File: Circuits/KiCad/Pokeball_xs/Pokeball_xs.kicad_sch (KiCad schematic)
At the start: 21 parts

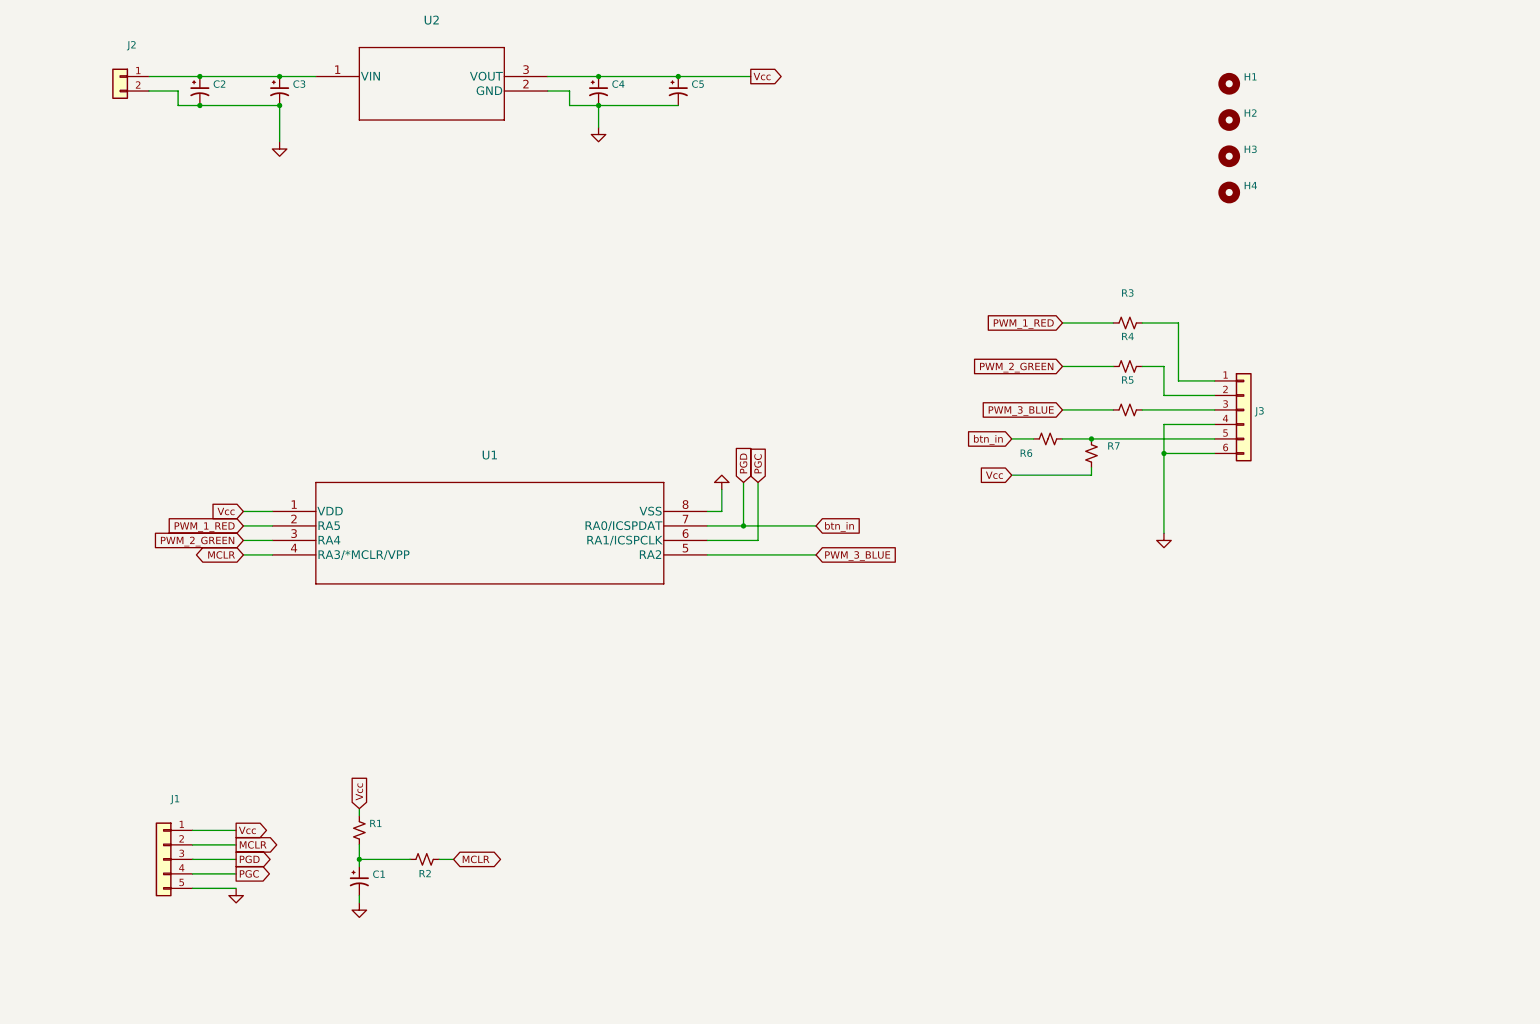
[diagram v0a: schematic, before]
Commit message: v 0.0.0.1 - Include the charging circuit on the PCB
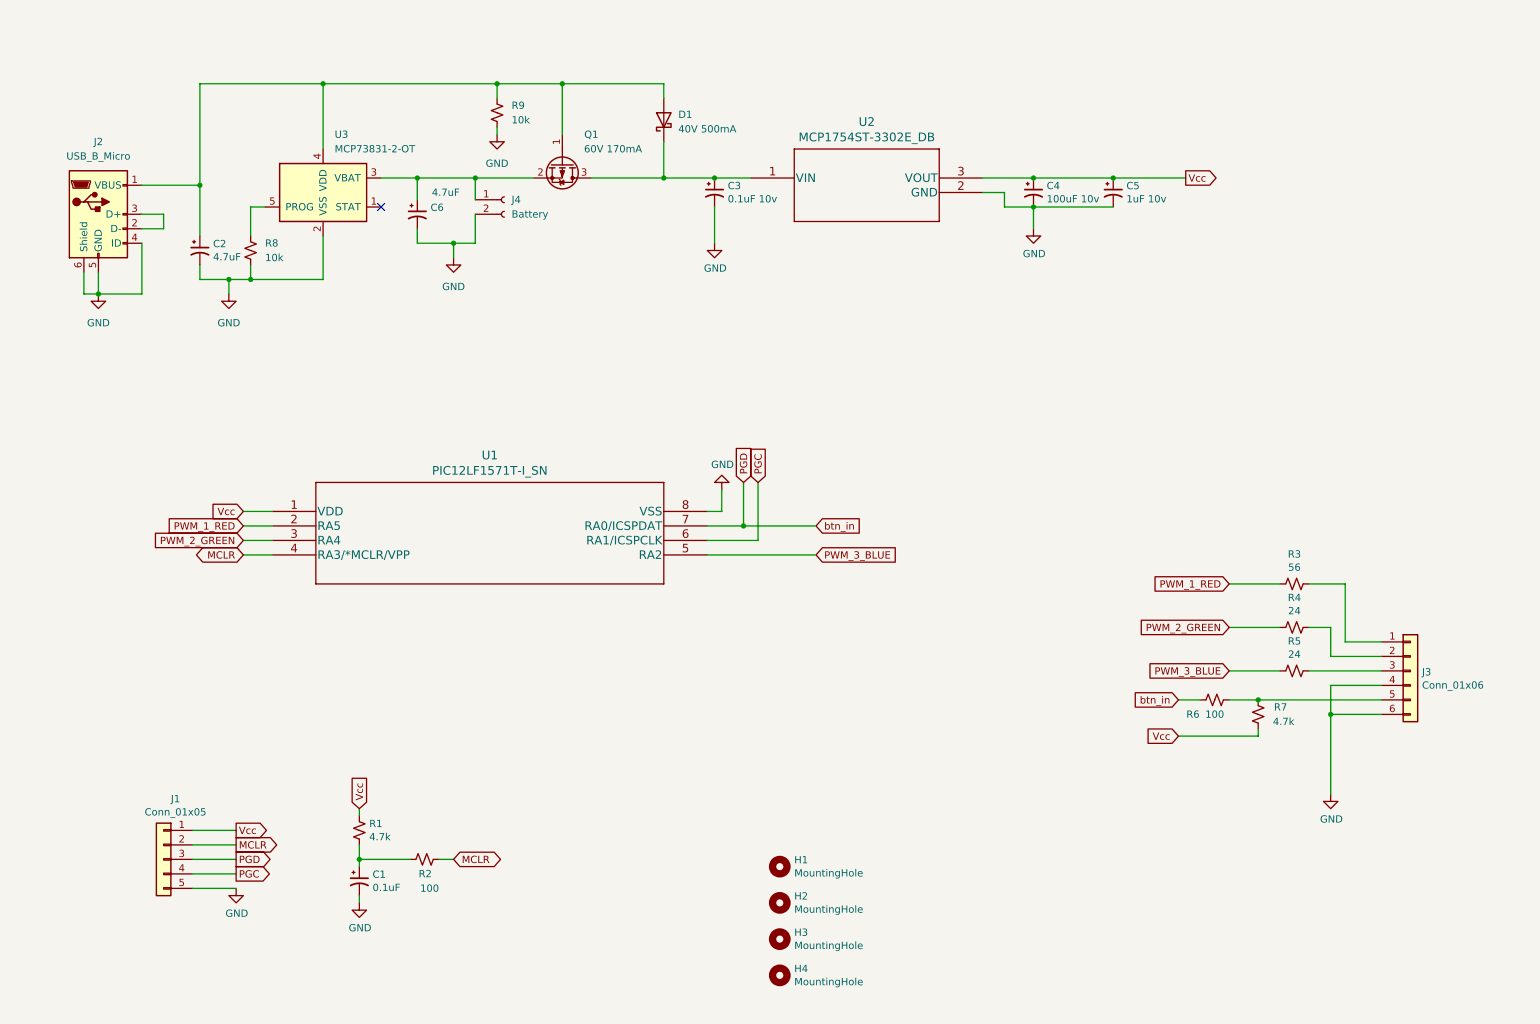
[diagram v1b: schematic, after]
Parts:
- removed J2: (no value), symbol Connector_Generic:Conn_01x02
- added C6: 4.7uF, Capacitor_SMD:C_0603_1608Metric, symbol Pokeball_xs-rescue:CP1_Small-Device
- added D1: 40V 500mA, Diode_SMD:D_SOD-123, symbol Device:D_Schottky
- added J2: USB_B_Micro, Connector_USB:USB_Micro-AB_Molex_47590-0001, symbol Connector:USB_B_Micro
- added J4: Battery, Connector_PinSocket_2.54mm:PinSocket_1x02_P2.54mm_Vertical, symbol Connector:Conn_01x02_Female
- added Q1: 60V 170mA, Package_TO_SOT_SMD:TSOT-23, symbol Device:Q_PMOS_GSD
- added R8, R9: 10k, Resistor_SMD:R_0603_1608Metric, symbol Device:R_Small_US
- added U3: MCP73831-2-OT, Package_TO_SOT_SMD:SOT-23-5, symbol Battery_Management:MCP73831-2-OT
- C1: value (none) -> 0.1uF; footprint (none) -> Capacitor_SMD:C_0603_1608Metric
- C2: value (none) -> 4.7uF; footprint (none) -> Capacitor_SMD:C_0603_1608Metric
- C3: value (none) -> 0.1uF 10v; footprint (none) -> Capacitor_SMD:C_0603_1608Metric
- C4: value (none) -> 100uF 10v; footprint (none) -> Capacitor_SMD:C_0603_1608Metric
- C5: value (none) -> 1uF 10v; footprint (none) -> Capacitor_SMD:C_0603_1608Metric
- H1, H2, H3, H4: value (none) -> MountingHole; footprint (none) -> MountingHole:MountingHole_4.3mm_M4
- J1: value (none) -> Conn_01x05; footprint (none) -> Connector_PinHeader_1.00mm:PinHeader_1x05_P1.00mm_Vertical
- J3: value (none) -> Conn_01x06; footprint (none) -> Connector_PinHeader_1.00mm:PinHeader_1x06_P1.00mm_Vertical
- R1, R7: value (none) -> 4.7k; footprint (none) -> Resistor_SMD:R_0603_1608Metric
- R2, R6: value (none) -> 100; footprint (none) -> Resistor_SMD:R_0603_1608Metric
- R3: value (none) -> 56; footprint (none) -> Resistor_SMD:R_0603_1608Metric
- R4, R5: value (none) -> 24; footprint (none) -> Resistor_SMD:R_0603_1608Metric
- U1: value (none) -> PIC12LF1571T-I_SN; footprint (none) -> PIC12LF1571T-I_SN:PIC12LF1571T-I&slash_SN
- U2: value (none) -> MCP1754ST-3302E_DB; footprint (none) -> MCP1754ST-3302E_DB:MCP1754ST-3302E&slash_DB
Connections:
- net GND: now also C6.2, J2.4 (ID), J2.5 (GND), J2.6 (Shield), J4.2 (Pin_2), R8.2, R9.2, U3.2 (VSS)
- net at C3.1, U2.1 (VIN): now also D1.1 (K), Q1.3 (D); no longer C2.1
- new net: C2.1, D1.2 (A), J2.1 (VBUS), Q1.1 (G), R9.1, U3.4 (VDD)
- new net: C6.1, J4.1 (Pin_1), Q1.2 (S), U3.3 (VBAT)
- new net: R8.1, U3.5 (PROG)
- new net: J2.2 (D-), J2.3 (D+)
- no-connect marks 0 -> 1
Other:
- moved on the sheet: C3, C4, C5, H1, H2, H3, H4, J3, R3, R4, R5, R6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

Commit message: v 0.0.0.2 - Testing the pwm output on the switch. Creation of the README.md.
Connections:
- net PWM_1_RED renamed PWM_4_RED
- net PWM_2_GREEN renamed PWM_3_GREEN
- net PWM_3_BLUE renamed PWM_1_BLUE
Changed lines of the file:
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@@
     )
   )
-  (global_label "PWM_2_GREEN" (shape input) (at 234.95 127 180) (fields_autoplaced)
+  (global_label "PWM_3_GREEN" (shape input) (at 234.95 127 180) (fields_autoplaced)
     (effects (font (size 1.27 1.27)) (justify right))
-    (property "Intersheet References" "${INTERSHEET_REFS}" (id 0) (at 29.21 45.72 0)
-      (effects (font (size 1.27 1.27)) hide)
+    (property "Intersheet References" "${INTERSHEET_REFS}" (id 0) (at 219.1396 126.9206 0)
+      (effects (font (size 1.27 1.27)) (justify right) hide)
     )
   )
@@
     )
   )
-  (global_label "PWM_3_BLUE" (shape input) (at 234.95 134.62 180) (fields_autoplaced)
+  (global_label "PWM_1_BLUE" (shape input) (at 234.95 134.62 180) (fields_autoplaced)
     (effects (font (size 1.27 1.27)) (justify right))
-    (property "Intersheet References" "${INTERSHEET_REFS}" (id 0) (at 29.21 45.72 0)
-      (effects (font (size 1.27 1.27)) hide)
+    (property "Intersheet References" "${INTERSHEET_REFS}" (id 0) (at 220.5306 134.5406 0)
+      (effects (font (size 1.27 1.27)) (justify right) hide)
     )
   )
-  (global_label "PWM_2_GREEN" (shape input) (at 62.23 111.76 180) (fields_autoplaced)
+  (global_label "PWM_3_GREEN" (shape input) (at 62.23 111.76 180) (fields_autoplaced)
     (effects (font (size 1.27 1.27)) (justify right))
-    (property "Intersheet References" "${INTERSHEET_REFS}" (id 0) (at 0 0 0)
-      (effects (font (size 1.27 1.27)) hide)
+    (property "Intersheet References" "${INTERSHEET_REFS}" (id 0) (at 46.4196 111.6806 0)
+      (effects (font (size 1.27 1.27)) (justify right) hide)
     )
   )
@@
     )
   )
-  (global_label "PWM_1_RED" (shape input) (at 234.95 119.38 180) (fields_autoplaced)
+  (global_label "PWM_4_RED" (shape input) (at 234.95 119.38 180) (fields_autoplaced)
     (effects (font (size 1.27 1.27)) (justify right))
-    (property "Intersheet References" "${INTERSHEET_REFS}" (id 0) (at 29.21 45.72 0)
-      (effects (font (size 1.27 1.27)) hide)
+    (property "Intersheet References" "${INTERSHEET_REFS}" (id 0) (at 221.6191 119.3006 0)
+      (effects (font (size 1.27 1.27)) (justify right) hide)
     )
   )
@@
     )
   )
-  (global_label "PWM_3_BLUE" (shape input) (at 162.56 114.3 0) (fields_autoplaced)
+  (global_label "PWM_1_BLUE" (shape input) (at 162.56 114.3 0) (fields_autoplaced)
     (effects (font (size 1.27 1.27)) (justify left))
-    (property "Intersheet References" "${INTERSHEET_REFS}" (id 0) (at 0 0 0)
-      (effects (font (size 1.27 1.27)) hide)
+    (property "Intersheet References" "${INTERSHEET_REFS}" (id 0) (at 176.9794 114.2206 0)
+      (effects (font (size 1.27 1.27)) (justify left) hide)
     )
   )
-  (global_label "PWM_1_RED" (shape input) (at 62.23 109.22 180) (fields_autoplaced)
+  (global_label "PWM_4_RED" (shape input) (at 62.23 109.22 180) (fields_autoplaced)
     (effects (font (size 1.27 1.27)) (justify right))
-    (property "Intersheet References" "${INTERSHEET_REFS}" (id 0) (at 0 0 0)
-      (effects (font (size 1.27 1.27)) hide)
+    (property "Intersheet References" "${INTERSHEET_REFS}" (id 0) (at 48.8991 109.1406 0)
+      (effects (font (size 1.27 1.27)) (justify right) hide)
     )
   )

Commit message: v 0.0.0.3 - updates to the board and the mechanical system.
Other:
- note added: "Might need to use internal pull up on btn_in. Vcc might pull up PGD. Maybe just don't populate R7."
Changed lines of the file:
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@@
     (stroke (width 0) (type default) (color 0 0 0 0))
+  )
+  (text "Might need to use internal pull up on btn_in. \nVcc might pull up PGD.\nMaybe just don't populate R7."
+    (at 199.39 156.21 0)
+    (effects (font (size 1.27 1.27)) (justify left bottom))
   )
   (global_label "MCLR" (shape output) (at 60.96 165.1 0) (fields_autoplaced)

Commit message: v 0.0.0.5 - updates to some circuit admin stuff
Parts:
- C3: value 0.1uF 10v -> 0.1uF
- C4: value 100uF 10v -> 22uF
- C5: value 1uF 10v -> 1uF
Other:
- note added: "1"
- note added: "8/25/2022"
- note added: "Engineer: Justin Knapp"
- note added: "ID might need to be floating instead of connected to ground."
- note added: "Pokeball_xs"
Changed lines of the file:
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@@
     (stroke (width 0) (type default) (color 0 0 0 0))
+  )
+  (text "ID might need to be floating instead of connected to ground."
+    (at 21.59 80.01 0)
+    (effects (font (size 1.27 1.27)) (justify left bottom))
+  )
+  (text "8/25/2022" (at 206.7279 193.969 0)
+    (effects (font (size 1.27 1.27)) (justify left bottom))
+  )
+  (text "Pokeball_xs" (at 186.69 190.5 0)
+    (effects (font (size 1.27 1.27)) (justify left bottom))
   )
   (text "Might need to use internal pull up on btn_in. \nVcc might pull up PGD.\nMaybe just don't populate R7."
     (at 199.39 156.21 0)
+    (effects (font (size 1.27 1.27)) (justify left bottom))
+  )
+  (text "Engineer: Justin Knapp" (at 260.35 185.42 0)
+    (effects (font (size 1.27 1.27)) (justify left bottom))
+  )
+  (text "1" (at 268.9325 194.05 0)
     (effects (font (size 1.27 1.27)) (justify left bottom))
   )
@@
       (effects (font (size 1.27 1.27)) (justify left))
     )
-    (property "Value" "1uF 10v" (id 1) (at 216.9414 51.943 0)
+    (property "Value" "1uF" (id 1) (at 216.9414 51.943 0)
       (effects (font (size 1.27 1.27)) (justify left))
     )
@@
       (effects (font (size 1.27 1.27)) (justify left))
     )
-    (property "Value" "100uF 10v" (id 1) (at 202.9714 51.943 0)
+    (property "Value" "22uF" (id 1) (at 202.9714 51.943 0)
       (effects (font (size 1.27 1.27)) (justify left))
     )
@@
       (effects (font (size 1.27 1.27)) (justify left))
     )
-    (property "Value" "0.1uF 10v" (id 1) (at 147.0914 51.943 0)
+    (property "Value" "0.1uF" (id 1) (at 147.0914 51.943 0)
       (effects (font (size 1.27 1.27)) (justify left))
     )
@@
     )
     (path "/00000000-0000-0000-0000-000062f599df"
-      (reference "C3") (unit 1) (value "0.1uF 10v") (footprint "Capacitor_SMD:C_0603_1608Metric")
+      (reference "C3") (unit 1) (value "0.1uF") (footprint "Capacitor_SMD:C_0603_1608Metric")
     )
     (path "/00000000-0000-0000-0000-000062f55fbb"
-      (reference "C4") (unit 1) (value "100uF 10v") (footprint "Capacitor_SMD:C_0603_1608Metric")
+      (reference "C4") (unit 1) (value "22uF") (footprint "Capacitor_SMD:C_0603_1608Metric")
     )
     (path "/00000000-0000-0000-0000-000062f55b37"
-      (reference "C5") (unit 1) (value "1uF 10v") (footprint "Capacitor_SMD:C_0603_1608Metric")
+      (reference "C5") (unit 1) (value "1uF") (footprint "Capacitor_SMD:C_0603_1608Metric")
     )
     (path "/d6912eff-a768-4791-81d8-17c7c13a387b"

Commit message: v 0.0.0.6 - Testing the circuit
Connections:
- net PWM_1_BLUE renamed PWM_3_BLUE
- net PWM_3_GREEN renamed PWM_2_GREEN
- net PWM_4_RED renamed PWM_1_RED
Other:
- note added: "Need dot on controller to indicate pin 1"
- note added: "Need to change the pinning of the USB."
- note added: "Need to make the connecting pins bigger."
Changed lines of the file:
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@@
+    (effects (font (size 1.27 1.27)) (justify left bottom))
+  )
+  (text "Need to change the pinning of the USB." (at 31.75 139.7 0)
+    (effects (font (size 1.27 1.27)) (justify left bottom))
+  )
+  (text "Need dot on controller to indicate pin 1" (at 31.75 137.16 0)
     (effects (font (size 1.27 1.27)) (justify left bottom))
   )
   (text "Pokeball_xs" (at 186.69 190.5 0)
+    (effects (font (size 1.27 1.27)) (justify left bottom))
+  )
+  (text "Need to make the connecting pins bigger." (at 31.75 142.24 0)
     (effects (font (size 1.27 1.27)) (justify left bottom))
   )
@@
     )
   )
-  (global_label "PWM_3_GREEN" (shape input) (at 234.95 127 180) (fields_autoplaced)
+  (global_label "PWM_2_GREEN" (shape input) (at 234.95 127 180) (fields_autoplaced)
     (effects (font (size 1.27 1.27)) (justify right))
     (property "Intersheet References" "${INTERSHEET_REFS}" (id 0) (at 219.1396 126.9206 0)
@@
     )
   )
-  (global_label "PWM_1_BLUE" (shape input) (at 234.95 134.62 180) (fields_autoplaced)
+  (global_label "PWM_3_BLUE" (shape input) (at 234.95 134.62 180) (fields_autoplaced)
     (effects (font (size 1.27 1.27)) (justify right))
     (property "Intersheet References" "${INTERSHEET_REFS}" (id 0) (at 220.5306 134.5406 0)
@@
     )
   )
-  (global_label "PWM_3_GREEN" (shape input) (at 62.23 111.76 180) (fields_autoplaced)
+  (global_label "PWM_2_GREEN" (shape input) (at 62.23 111.76 180) (fields_autoplaced)
     (effects (font (size 1.27 1.27)) (justify right))
     (property "Intersheet References" "${INTERSHEET_REFS}" (id 0) (at 46.4196 111.6806 0)
@@
     )
   )
-  (global_label "PWM_4_RED" (shape input) (at 234.95 119.38 180) (fields_autoplaced)
+  (global_label "PWM_1_RED" (shape input) (at 234.95 119.38 180) (fields_autoplaced)
     (effects (font (size 1.27 1.27)) (justify right))
     (property "Intersheet References" "${INTERSHEET_REFS}" (id 0) (at 221.6191 119.3006 0)
@@
     )
   )
-  (global_label "PWM_1_BLUE" (shape input) (at 162.56 114.3 0) (fields_autoplaced)
+  (global_label "PWM_3_BLUE" (shape input) (at 162.56 114.3 0) (fields_autoplaced)
     (effects (font (size 1.27 1.27)) (justify left))
     (property "Intersheet References" "${INTERSHEET_REFS}" (id 0) (at 176.9794 114.2206 0)
@@
     )
   )
-  (global_label "PWM_4_RED" (shape input) (at 62.23 109.22 180) (fields_autoplaced)
+  (global_label "PWM_1_RED" (shape input) (at 62.23 109.22 180) (fields_autoplaced)
     (effects (font (size 1.27 1.27)) (justify right))
     (property "Intersheet References" "${INTERSHEET_REFS}" (id 0) (at 48.8991 109.1406 0)

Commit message: v 0.0.0.8 - Board submitted to pcbway
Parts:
- removed R7: 4.7k, Resistor_SMD:R_0603_1608Metric, symbol Device:R_Small_US
- added C7: 47uF, Capacitor_SMD:C_0603_1608Metric, symbol Pokeball_xs-rescue:CP1_Small-Device
- added C8: 22uF, Capacitor_SMD:C_0603_1608Metric, symbol Pokeball_xs-rescue:CP1_Small-Device
- C4: value 22uF -> 47uF
- J1: footprint Connector_PinHeader_1.00mm:PinHeader_1x05_P1.00mm_Vertical -> Connector_PinHeader_2.00mm:PinHeader_1x05_P2.00mm_Vertical
- J2: footprint Connector_USB:USB_Micro-AB_Molex_47590-0001 -> Connector_USB:USB_Micro-B_Molex-105017-0001
- J3: footprint Connector_PinHeader_1.00mm:PinHeader_1x06_P1.00mm_Vertical -> Connector_PinHeader_2.00mm:PinHeader_1x06_P2.00mm_Vertical
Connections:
- net GND: now also C7.2, C8.2
- net Vcc: now also C7.1, C8.1
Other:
- note removed: "ID might need to be floating instead of connected to ground."
- note removed: "Might need to use internal pull up on btn_in. Vcc might pull up PGD. Maybe just don't populate R7."
- moved on the sheet: C5
